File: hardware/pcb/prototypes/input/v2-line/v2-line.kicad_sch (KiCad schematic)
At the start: 51 parts, among them J1 PH, J2 ANLG, J3 LOWV, J4 GND, J5 TRS, J6 XLR, J7 SW CTRL, J8 OUT_BIAS, J9 OUT, SW1 DG1412EEQ, U1 INA1650, U2 OPA1612AxD, U3 OPA1637

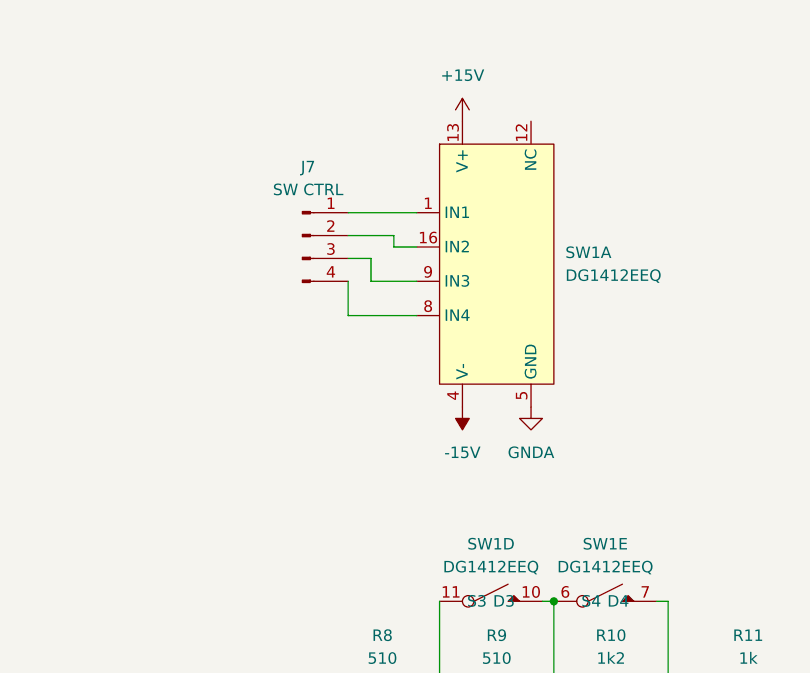
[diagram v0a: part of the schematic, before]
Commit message: add decoupling caps to sw
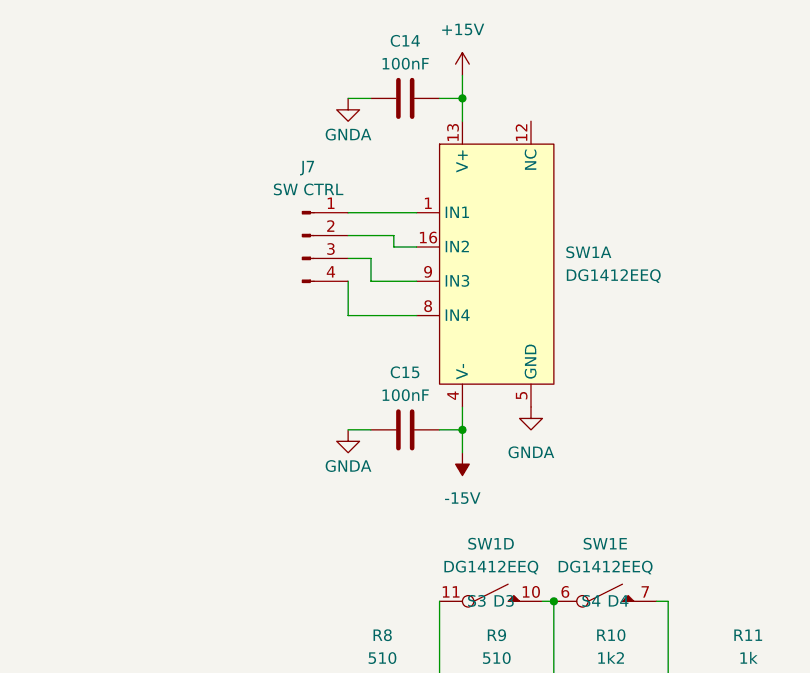
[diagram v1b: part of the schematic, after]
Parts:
- added C14, C15: 100nF, Capacitor_SMD:C_0805_2012Metric_Pad1.18x1.45mm_HandSolder, symbol Device:C
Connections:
- net +15V: now also C14.2
- net -15V: now also C15.2
- net Earth: now also C14.1, C15.1

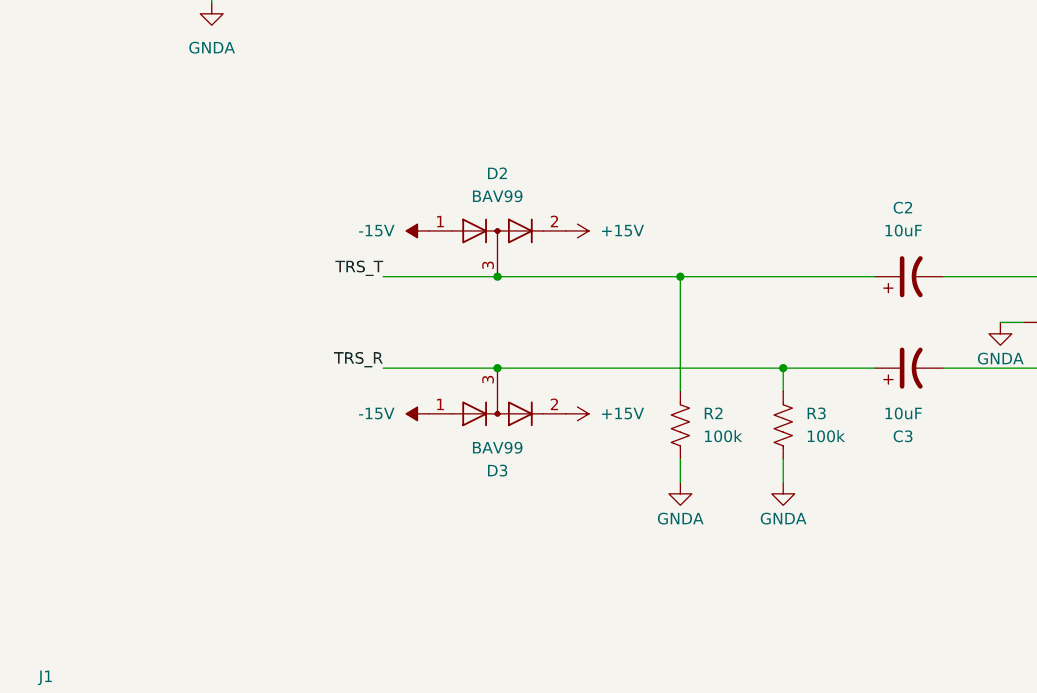
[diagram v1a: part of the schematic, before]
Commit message: add RFI protection
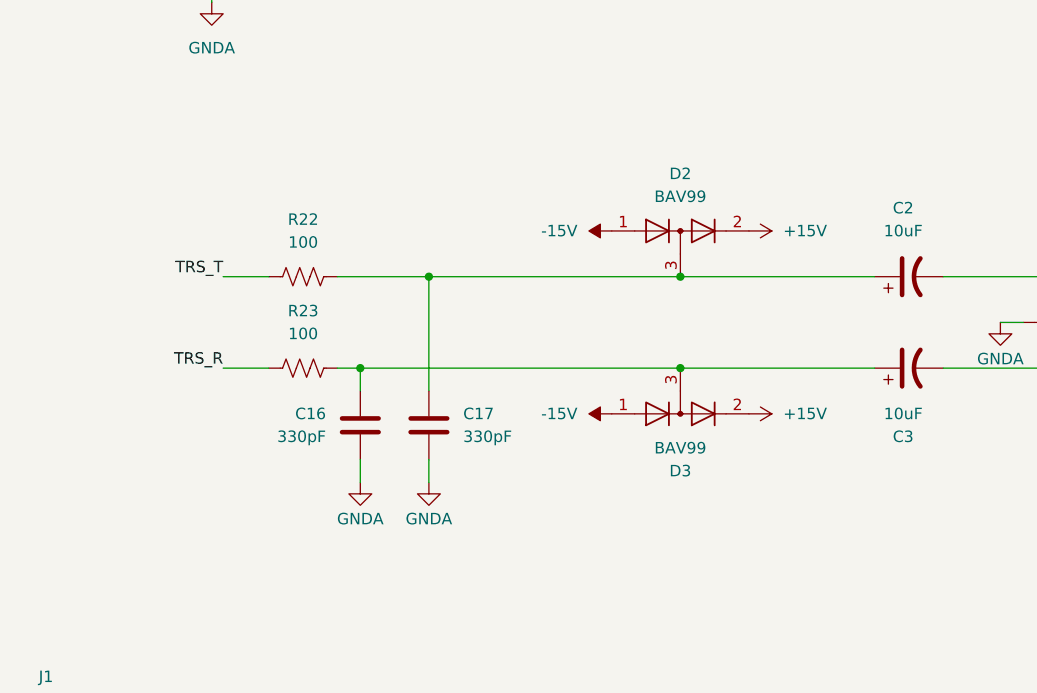
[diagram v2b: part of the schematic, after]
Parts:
- removed R2, R3: 100k, Resistor_SMD:R_0805_2012Metric_Pad1.20x1.40mm_HandSolder, symbol Device:R_US
- added C16, C17: 330pF, Capacitor_SMD:C_0805_2012Metric_Pad1.18x1.45mm_HandSolder, symbol Device:C
- added R22, R23: 100, Resistor_SMD:R_0805_2012Metric_Pad1.20x1.40mm_HandSolder, symbol Device:R_US
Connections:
- net Earth: now also C16.2, C17.2
- net TRS_R: now also R23.2; no longer C3.1, D3.3 (K)
- net TRS_T: now also R22.2; no longer C2.1, D2.3 (K)
- new net: C16.1, C3.1, D3.3 (K), R23.1
- new net: C17.1, C2.1, D2.3 (K), R22.1
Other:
- moved on the sheet: D2, D3
